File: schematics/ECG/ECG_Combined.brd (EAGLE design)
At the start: 25.4 x 25.4 mm, 72 parts, among them IC1 ADS1293, IC2 LIS3DH, IC3 MCP1703, IC4 CC2541, IC5 FSA4157, IC6 FSA4157, IC7 FSA4157, X1 XTAL-2SMD, X2 XTAL_403, X3 XTAL-CSM7

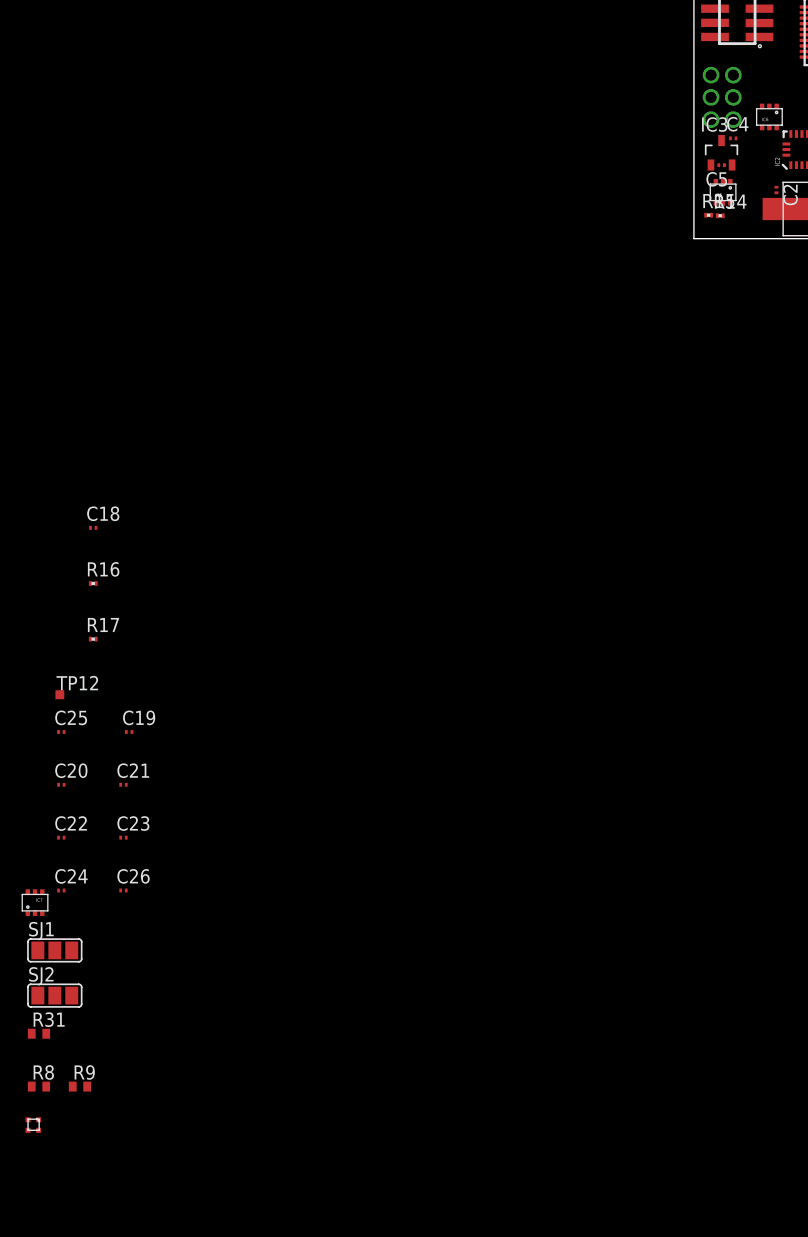
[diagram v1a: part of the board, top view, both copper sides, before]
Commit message: replaced 6 pin power header with 4 pin. added ESD protection diodes to circuit input
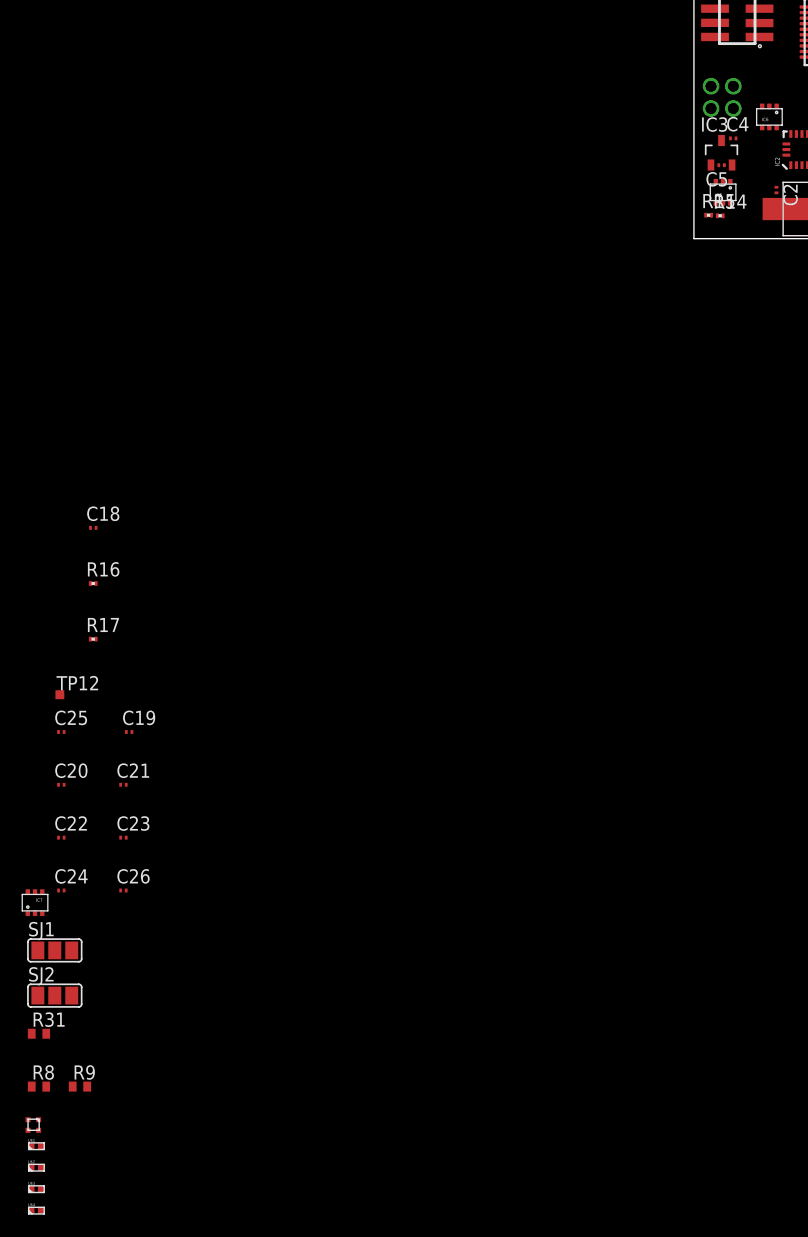
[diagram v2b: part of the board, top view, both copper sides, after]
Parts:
- added U$1, U$2, U$3, U$4: ZD_0402, semtech:0402
- CONN2: value M80-6V -> M80-4V; device harwin:M80-6-V -> harwin:M80-4-V
- turned CONN2 to 180 degrees
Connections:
- net GND: now also U$1.1, U$2.1, U$3.1, U$4.1
- net LA: now also U$3.2
- net LL: now also U$2.2
- net RA: now also U$4.2
- net RL: now also U$1.2
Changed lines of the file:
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@@
 <element name="R14" library="rcl" package="R0201" value="100K" x="2.3622" y="2.0574"/>
 <element name="R15" library="rcl" package="R0201" value="100K" x="1.3208" y="2.1082"/>
-<element name="CONN2" library="harwin" package="M80-6-V" value="M80-6V" x="2.54" y="12.7" rot="R90"/>
 <element name="CONN3" library="harwin" package="M80-6-V" value="M80-6V" x="22.86" y="12.7" rot="R90"/>
 <element name="R1" library="rcl" package="R0201" value="0" x="20.6294" y="6.8632"/>
@@
 <element name="TRI_LED" library="lumex" package="SML-LX0404SIUPGUSB" value="SML-LX0404SIUPGUSB" x="-59.3598" y="-79.6544"/>
 <element name="R9" library="rcl" package="R0402" value="1K" x="-55.1942" y="-76.2254"/>
+<element name="CONN2" library="harwin" package="M80-4-V" value="M80-4V" x="2.54" y="12.7" rot="R180"/>
+<element name="U$1" library="semtech" package="0402" value="ZD_0402" x="-59.1058" y="-81.5848"/>
+<element name="U$2" library="semtech" package="0402" value="ZD_0402" x="-59.1058" y="-83.5152"/>
+<element name="U$3" library="semtech" package="0402" value="ZD_0402" x="-59.1058" y="-85.4456"/>
+<element name="U$4" library="semtech" package="0402" value="ZD_0402" x="-59.1058" y="-87.376"/>
 </elements>
 <signals>
@@
 <contactref element="IC5" pad="3"/>
 <contactref element="R15" pad="1"/>
-<contactref element="CONN2" pad="2"/>
 <contactref element="C18" pad="2"/>
 <contactref element="IC6" pad="3"/>
@@
 <contactref element="IC7" pad="3"/>
 <contactref element="IC7" pad="2"/>
+<contactref element="CONN2" pad="2"/>
+<contactref element="U$4" pad="1"/>
+<contactref element="U$3" pad="1"/>
+<contactref element="U$2" pad="1"/>
+<contactref element="U$1" pad="1"/>
+<wire x1="-59.5566" y1="-85.4456" x2="-59.5566" y2="-87.376" width="0" layer="19" extent="1-1"/>
+<wire x1="-59.5566" y1="-83.5152" x2="-59.5566" y2="-85.4456" width="0" layer="19" extent="1-1"/>
+<wire x1="-59.5566" y1="-81.5848" x2="-59.5566" y2="-83.5152" width="0" layer="19" extent="1-1"/>
+<wire x1="-55.9308" y1="-68.0466" x2="-59.5566" y2="-81.5848" width="0" layer="19" extent="1-1"/>
 <wire x1="-55.9308" y1="-63.9826" x2="-55.9308" y2="-68.0466" width="0" layer="19" extent="1-1"/>
 <wire x1="-58.582" y1="-60.64" x2="-55.9308" y2="-63.9826" width="0" layer="19" extent="1-1"/>
@@
 <wire x1="-40.39" y1="44.45" x2="-42.53" y2="34.29" width="0" layer="19" extent="1-1"/>
 <wire x1="-31.5" y1="49.53" x2="-40.39" y2="44.45" width="0" layer="19" extent="1-1"/>
-<wire x1="8.3566" y1="27.7154" x2="-23.88" y2="34.29" width="0" layer="19" extent="1-1"/>
-<wire x1="9.9314" y1="27.05" x2="8.3566" y2="27.7154" width="0" layer="19" extent="1-1"/>
-<wire x1="10.5918" y1="24.8372" x2="9.9314" y2="27.05" width="0" layer="19" extent="1-1"/>
-<wire x1="13.8852" y1="26.8508" x2="10.5918" y2="24.8372" width="0" layer="19" extent="1-1"/>
-<wire x1="14.859" y1="24.8372" x2="13.8852" y2="26.8508" width="0" layer="19" extent="1-1"/>
-<wire x1="9.9276" y1="20.8242" x2="10.5918" y2="24.8372" width="0" layer="19" extent="1-1"/>
-<wire x1="9.9276" y1="19.3242" x2="9.9276" y2="20.8242" width="0" layer="19" extent="1-1"/>
-<wire x1="12.9276" y1="18.5742" x2="9.9276" y2="19.3242" width="0" layer="19" extent="1-1"/>
-<wire x1="5.8954" y1="18.1308" x2="9.9276" y2="19.3242" width="0" layer="19" extent="1-1"/>
-<wire x1="3.54" y1="12.7" x2="5.8954" y2="18.1308" width="0" layer="19" extent="1-1"/>
-<wire x1="6.135" y1="11.8918" x2="3.54" y2="12.7" width="0" layer="19" extent="1-1"/>
+<wire x1="1.54" y1="13.7" x2="-23.88" y2="34.29" width="0" layer="19" extent="1-1"/>
+<wire x1="6.135" y1="11.8918" x2="1.54" y2="13.7" width="0" layer="19" extent="1-1"/>
 <wire x1="6.785" y1="11.8918" x2="6.135" y2="11.8918" width="0" layer="19" extent="1-1"/>
 <wire x1="9.214" y1="9.4082" x2="6.785" y2="11.8918" width="0" layer="19" extent="1-1"/>
 <wire x1="10.214" y1="9.4082" x2="9.214" y2="9.4082" width="0" layer="19" extent="1-1"/>
 <wire x1="10.714" y1="6.6082" x2="10.214" y2="9.4082" width="0" layer="19" extent="1-1"/>
-<wire x1="3.7806" y1="9.017" x2="3.54" y2="12.7" width="0" layer="19" extent="1-1"/>
+<wire x1="3.7806" y1="9.017" x2="6.135" y2="11.8918" width="0" layer="19" extent="1-1"/>
 <wire x1="2.2392" y1="6.604" x2="3.7806" y2="9.017" width="0" layer="19" extent="1-1"/>
 <wire x1="1.5304" y1="6.6208" x2="2.2392" y2="6.604" width="0" layer="19" extent="1-1"/>
@@
 <wire x1="19.4016" y1="18.0848" x2="18.8508" y2="12.9794" width="0" layer="19" extent="1-1"/>
 <wire x1="18.1538" y1="6.203" x2="15.6538" y2="11.003" width="0" layer="19" extent="1-1"/>
+<wire x1="5.8954" y1="18.1308" x2="1.54" y2="13.7" width="0" layer="19" extent="1-1"/>
+<wire x1="9.9276" y1="19.3242" x2="5.8954" y2="18.1308" width="0" layer="19" extent="1-1"/>
+<wire x1="9.9276" y1="20.8242" x2="9.9276" y2="19.3242" width="0" layer="19" extent="1-1"/>
+<wire x1="12.9276" y1="18.5742" x2="9.9276" y2="19.3242" width="0" layer="19" extent="1-1"/>
+<wire x1="10.5918" y1="24.8372" x2="9.9276" y2="20.8242" width="0" layer="19" extent="1-1"/>
+<wire x1="9.9314" y1="27.05" x2="10.5918" y2="24.8372" width="0" layer="19" extent="1-1"/>
+<wire x1="8.3566" y1="27.7154" x2="9.9314" y2="27.05" width="0" layer="19" extent="1-1"/>
+<wire x1="13.8852" y1="26.8508" x2="10.5918" y2="24.8372" width="0" layer="19" extent="1-1"/>
+<wire x1="14.859" y1="24.8372" x2="13.8852" y2="26.8508" width="0" layer="19" extent="1-1"/>
 </signal>
 <signal name="IN1">
@@
 <contactref element="R1" pad="2"/>
 <contactref element="CONN3" pad="1"/>
-<wire x1="20.8844" y1="6.8632" x2="23.86" y2="10.7" width="0" layer="19" extent="1-1"/>
+<contactref element="U$4" pad="2"/>
+<wire x1="20.8844" y1="6.8632" x2="-58.7066" y2="-87.376" width="0" layer="19" extent="1-1"/>
+<wire x1="23.86" y1="10.7" x2="20.8844" y2="6.8632" width="0" layer="19" extent="1-1"/>
 <wire x1="-34.29" y1="53.34" x2="23.86" y2="10.7" width="0" layer="19" extent="1-1"/>
 </signal>
@@
 <contactref element="R2" pad="2"/>
 <contactref element="CONN3" pad="3"/>
-<wire x1="20.8844" y1="8.0392" x2="23.86" y2="14.7" width="0" layer="19" extent="1-1"/>
+<contactref element="U$2" pad="2"/>
+<wire x1="20.8844" y1="8.0392" x2="-58.7066" y2="-83.5152" width="0" layer="19" extent="1-1"/>
+<wire x1="23.86" y1="14.7" x2="20.8844" y2="8.0392" width="0" layer="19" extent="1-1"/>
 <wire x1="-44.45" y1="53.34" x2="23.86" y2="14.7" width="0" layer="19" extent="1-1"/>
 </signal>
@@
 <contactref element="R4" pad="2"/>
 <contactref element="CONN3" pad="6"/>
-<wire x1="20.8844" y1="8.6018" x2="21.86" y2="10.7" width="0" layer="19" extent="1-1"/>
+<contactref element="U$1" pad="2"/>
+<wire x1="20.8844" y1="8.6018" x2="-58.7066" y2="-81.5848" width="0" layer="19" extent="1-1"/>
+<wire x1="21.86" y1="10.7" x2="20.8844" y2="8.6018" width="0" layer="19" extent="1-1"/>
 <wire x1="-49.53" y1="53.34" x2="21.86" y2="10.7" width="0" layer="19" extent="1-1"/>
 </signal>
@@
 <contactref element="R12" pad="2"/>
 <contactref element="CONN3" pad="2"/>
-<wire x1="20.8844" y1="7.4512" x2="23.86" y2="12.7" width="0" layer="19" extent="1-1"/>
+<contactref element="U$3" pad="2"/>
+<wire x1="20.8844" y1="7.4512" x2="-58.7066" y2="-85.4456" width="0" layer="19" extent="1-1"/>
+<wire x1="23.86" y1="12.7" x2="20.8844" y2="7.4512" width="0" layer="19" extent="1-1"/>
 <wire x1="-39.37" y1="53.34" x2="23.86" y2="12.7" width="0" layer="19" extent="1-1"/>
 </signal>
@@
 <signal name="BATT">
 <contactref element="IC5" pad="1"/>
-<contactref element="CONN2" pad="1"/>
 <contactref element="IC3" pad="3"/>
 <contactref element="C4" pad="1"/>
-<wire x1="3.2806" y1="9.017" x2="3.54" y2="10.7" width="0" layer="19" extent="1-1"/>
-<wire x1="2.4804" y1="8.8208" x2="3.2806" y2="9.017" width="0" layer="19" extent="1-1"/>
-<wire x1="3.2714" y1="5.1152" x2="2.4804" y2="8.8208" width="0" layer="19" extent="1-1"/>
+<contactref element="CONN2" pad="1"/>
+<wire x1="3.2714" y1="5.1152" x2="3.54" y2="13.7" width="0" layer="19" extent="1-1"/>
+<wire x1="2.4804" y1="8.8208" x2="3.2714" y2="5.1152" width="0" layer="19" extent="1-1"/>
+<wire x1="3.2806" y1="9.017" x2="2.4804" y2="8.8208" width="0" layer="19" extent="1-1"/>
 </signal>
 <signal name="BATT_CHECK">

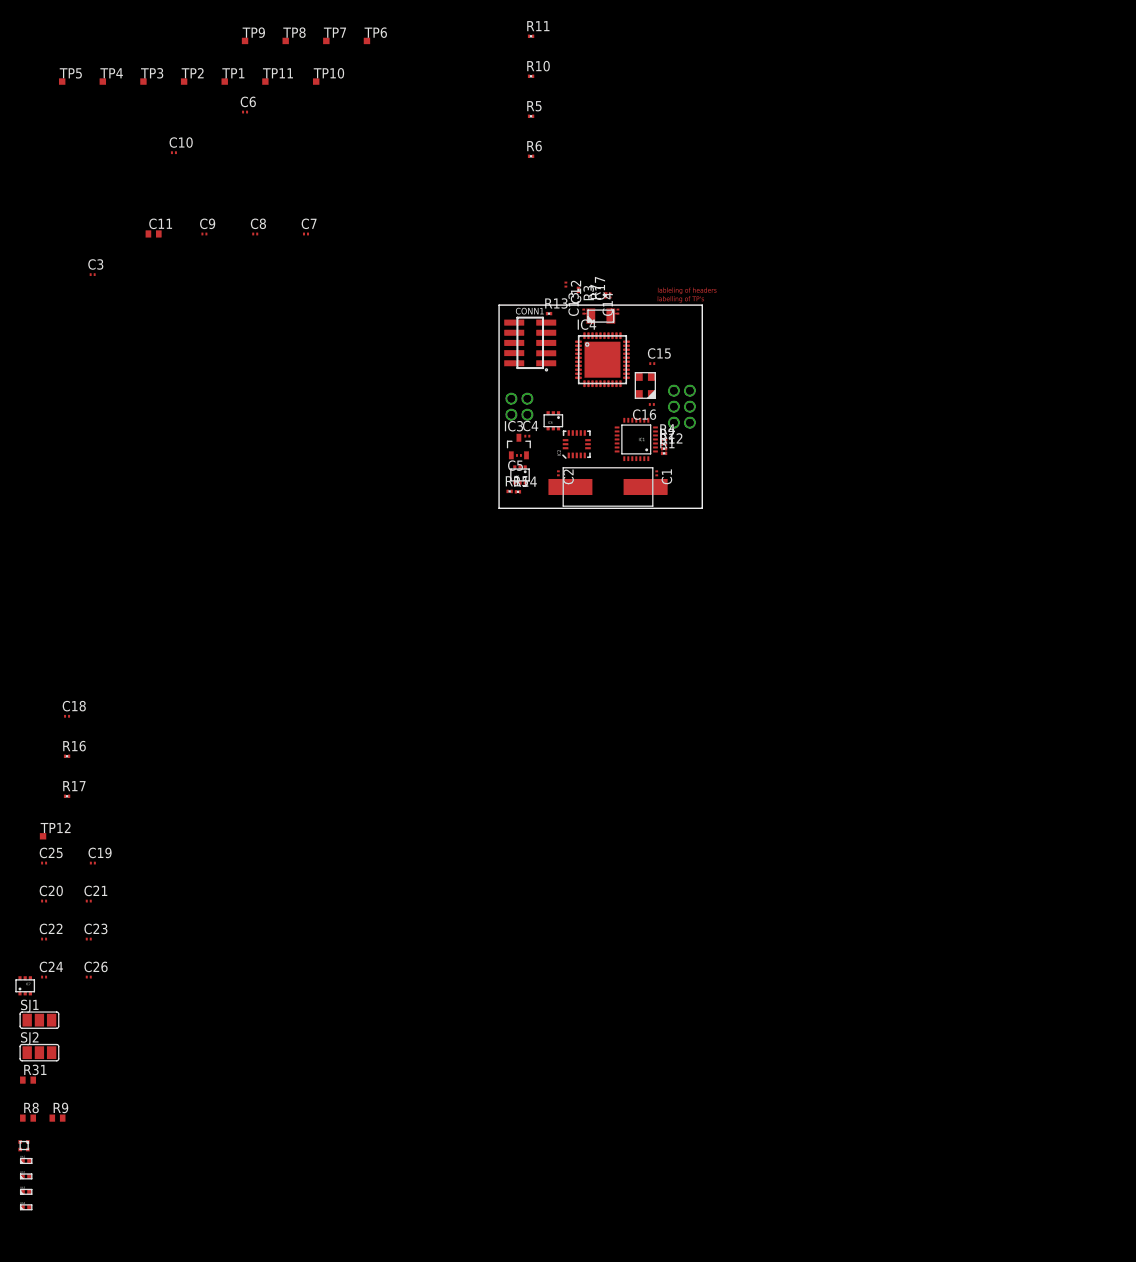
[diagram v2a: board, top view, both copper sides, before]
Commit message: removed cc2541 ground on pin 4. added balun and antenna
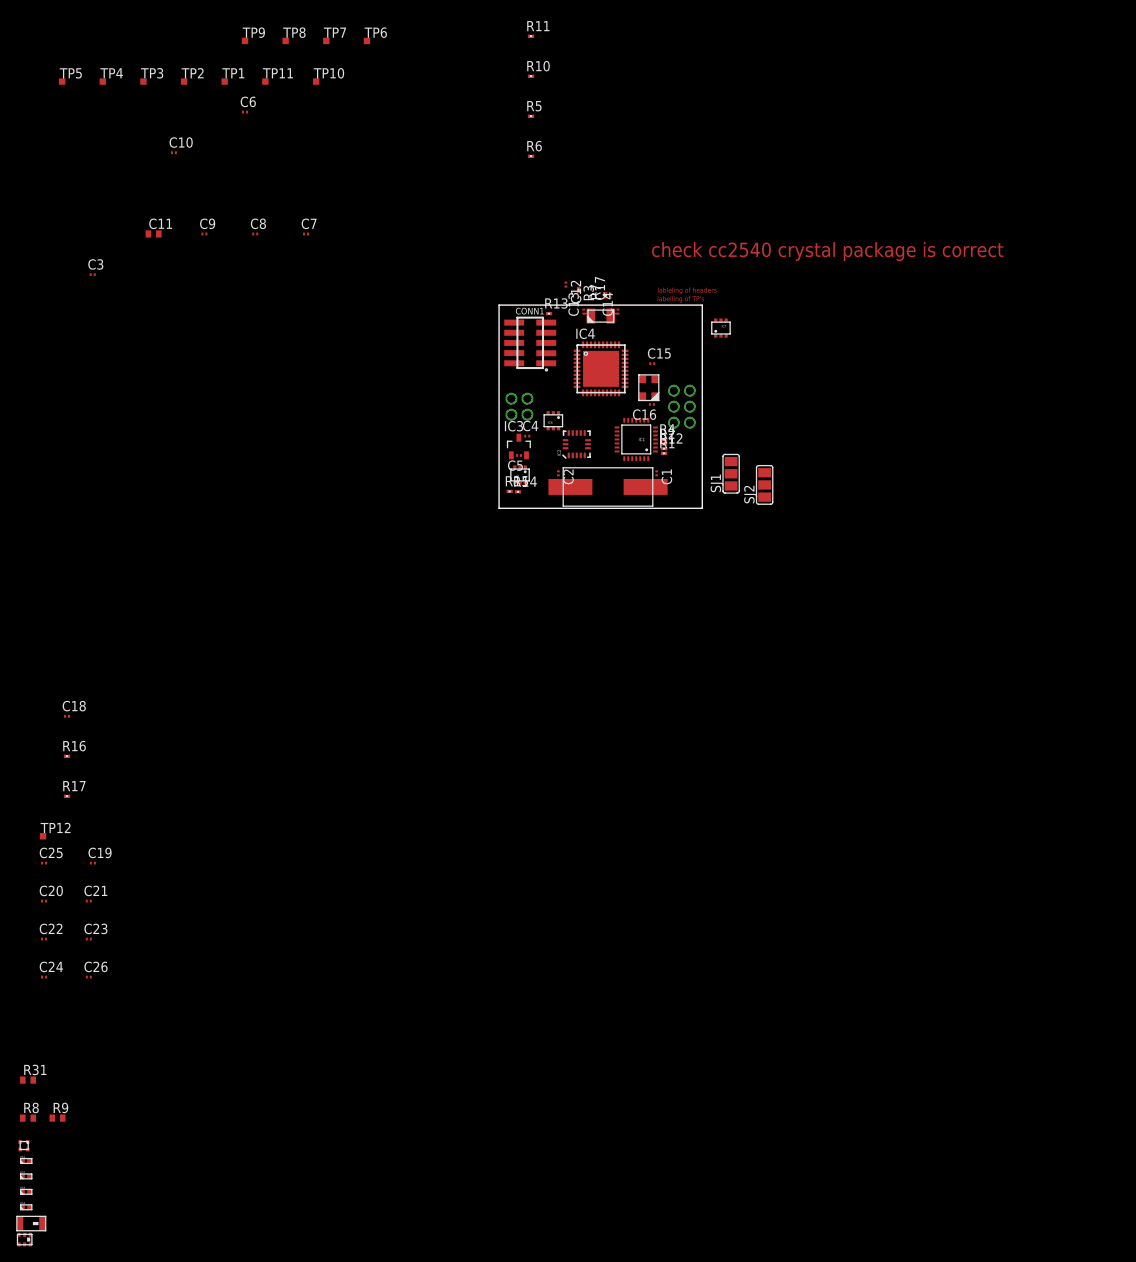
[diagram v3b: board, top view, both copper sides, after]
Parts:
- added IC8: (no value), johanson:BALUN_SMD_2450BM_SERIES
- added RF: ANTENNA_SMD, johanson:ANTENNA_SMD
- moved IC7 119.7 mm to (27.8, 22.5)
- moved SJ2 115.1 mm to (33.2, 2.92), turned to 90 degrees
- moved SJ1 110.2 mm to (29.0, 4.32), turned to 90 degrees
- moved IC4 1.16 mm to (12.7, 17.4)
- moved X2 0.51 mm to (18.7, 15.1)
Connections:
- net DCOUPL1 renamed DCOUPL
- removed net P1_2/DCDC: IC4.8
- new net N$6: IC8.1, RF.1
- new net N/C: IC4.4
- net GND: now also IC8.2, IC8.5, IC8.6; no longer IC4.4
- net RF_N: now also IC8.3
- net RF_P: now also IC8.4
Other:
- board text added: "check cc2540 crystal package is correct"
